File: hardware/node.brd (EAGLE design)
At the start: 39.4 x 25.7 mm, 74 parts, among them IC1 MAX1555, IC2 TS5205, Q1 P-MOSFET, U1 ATMEGA32U4, U2 MCP1703CB/TOREX-XC6206, Y1 8MHz

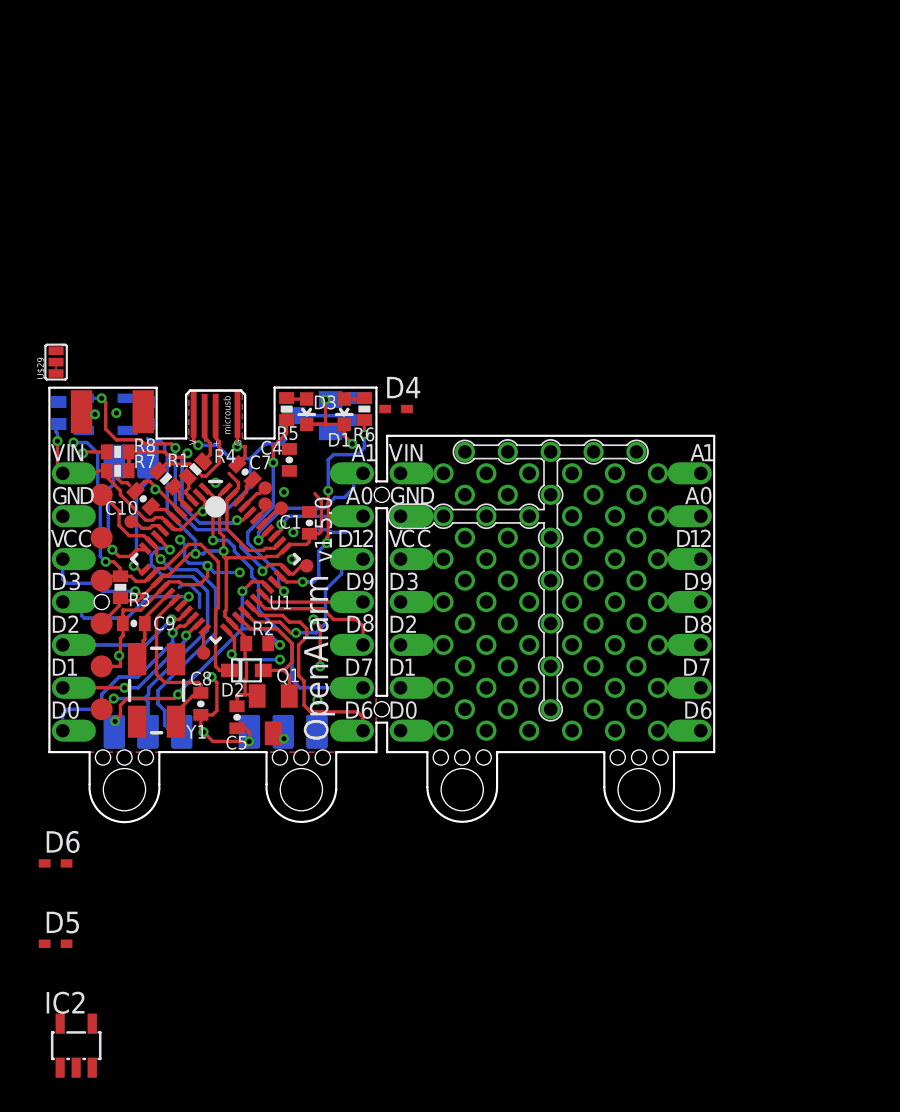
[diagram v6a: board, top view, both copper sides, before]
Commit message: Node + Proto Shield + Lipo Shield
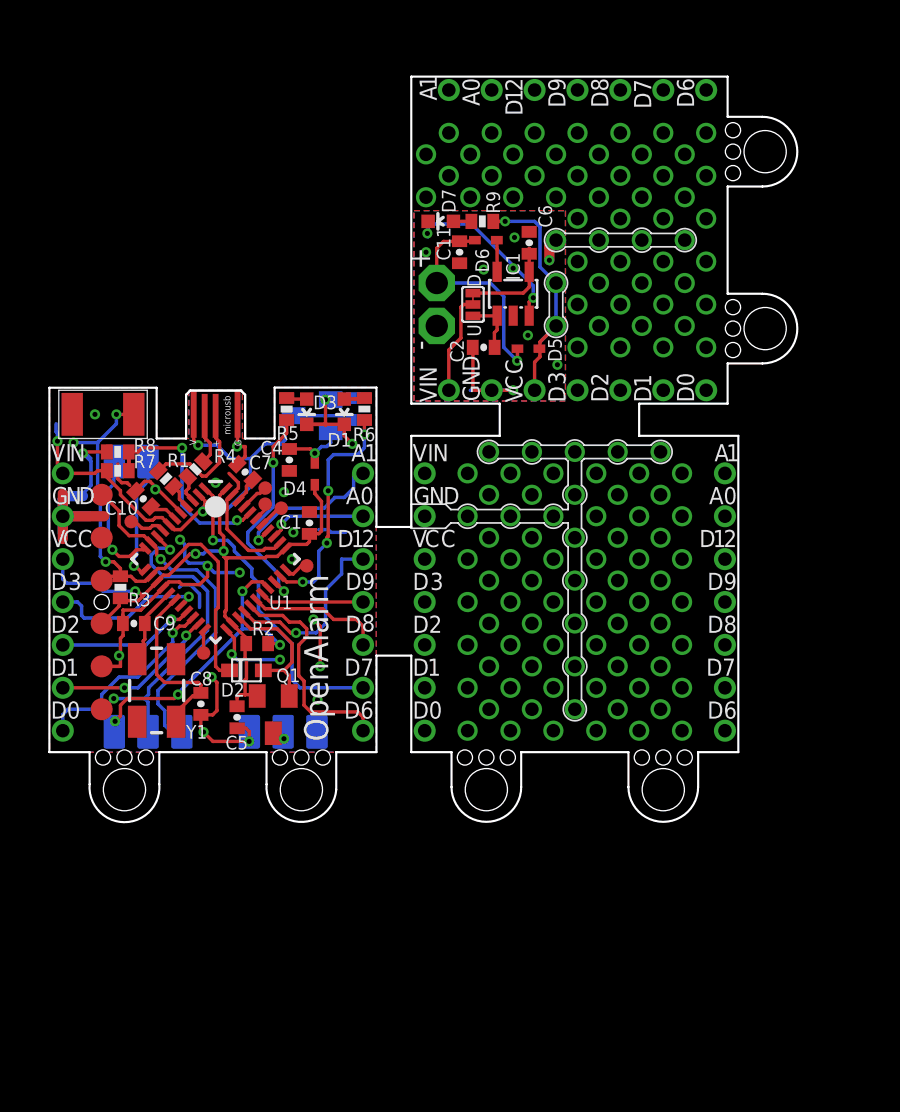
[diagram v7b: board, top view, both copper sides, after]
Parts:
- removed IC2: TS5205, v-reg:SOT25
- added C11: 1uF, SparkFun:0402-CAP
- added D7: Green, SparkFun:LED-0603
- added LIPO+, LIPO-: TPPAD1-13, testpad:P1-13
- added R9: 330, SparkFun:0402-RES
- added U$30, U$31, U$32, U$33, U$34, U$35, U$36, U$37, U$38, U$39, U$40, U$41, U$42, U$43: IOPAD, openalarm:IOPAD
- moved D5 45.1 mm to (28.4, 23.9), turned to 180 degrees
- moved D6 44.8 mm to (25.8, 30.3)
- moved C2 25.5 mm to (25.7, 24.0), flipped to the top, turned to 0 degrees
- moved IC1 25.2 mm to (27.5, 27.1), flipped to the top, turned to 0 degrees
- moved U$29 24.9 mm to (25.1, 26.5), turned to 270 degrees
- moved C6 24.8 mm to (28.4, 30.2), flipped to the top
- moved D4 6.15 mm to (15.7, 16.4), turned to 90 degrees
- moved U$15 1.43 mm to (22.7, 16.5)
- moved U$16 1.43 mm to (22.7, 14.0)
- moved U$17 1.43 mm to (22.7, 11.4)
- moved U$18 1.43 mm to (22.7, 8.89)
- moved U$19 1.43 mm to (22.7, 6.35)
- moved U$20 1.43 mm to (22.7, 3.81)
- moved U$21 1.43 mm to (22.7, 1.27)
- moved U$22 1.43 mm to (39.5, 1.27)
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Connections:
- removed net CHG: IC1.3, TP12.TP, U1.33
- removed net N$12: C6.2, D5.A, D6.C
- removed net N$14: IC1.4, U$29.C0
- removed net N$15: C2.2, U$29.COM
- new net N$133: D7.C, IC1.3
- new net N$178: C6.2, IC1.4, U$29.C0
- new net N$179: C2.2, IC1.1, U$29.C1
- new net N$181: U$33.P$1
- new net N$182: U$34.P$1
- new net N$183: U$35.P$1
- new net N$184: U$36.P$1
- new net N$185: U$38.P$1
- new net N$186: U$39.P$1
- new net N$187: U$40.P$1
- new net N$188: U$41.P$1
- new net N$189: U$42.P$1
- new net N$190: U$43.P$1
- new net N$191: U$37.P$1
- new net N$192: C11.2, D5.A, D6.C, LIPO+.TP
- new net SL_GND: C11.1, C2.1, C6.1, IC1.2, LIPO-.TP, U$31.P$1
- new net SL_VBUS: U$29.COM, U$30.P$1
- new net SL_VCC: D5.C, R9.2, U$32.P$1
- new net _CHG: TP12.TP, U1.33
- net A0: now also U$9.P$1; no longer U$9.P$2
- net A1: now also U$8.P$1; no longer U$8.P$2
- net D0: now also U$2.P$1; no longer U$2.P$2
- net D1: now also U$1.P$1; no longer U$1.P$2
- net D12: now also U$10.P$1; no longer U$10.P$2
- net D2: now also U$3.P$1; no longer U$3.P$2
- net D3: now also U$4.P$1; no longer U$4.P$2
- net D6: now also U$14.P$1; no longer U$14.P$2
- net D7: now also U$13.P$1; no longer U$13.P$2
- net D8: now also U$12.P$1; no longer U$12.P$2
- net D9: now also U$11.P$1; no longer U$11.P$2
- net GND: now also U$6.P$1; no longer C2.1, C6.1, IC1.2, U$6.P$2
- net N$11: now also D7.A, R9.1; no longer IC1.1, U$29.C1
- net N$13: now also U$16.P$1; no longer U$16.P$2
- net N$27: now also U$17.P$1; no longer U$17.P$2
- net N$29: now also U$18.P$1; no longer U$18.P$2
- net N$30: now also U$19.P$1; no longer U$19.P$2
- net N$31: now also U$20.P$1; no longer U$20.P$2
- net N$32: now also U$21.P$1; no longer U$21.P$2
- net N$40: now also U$23.P$1; no longer U$23.P$2
- net N$41: now also U$24.P$1; no longer U$24.P$2
- net N$42: now also U$25.P$1; no longer U$25.P$2
- net N$43: now also U$26.P$1; no longer U$26.P$2
- net N$44: now also U$27.P$1; no longer U$27.P$2
- net N$45: now also U$28.P$1; no longer U$28.P$2
- net N$46: now also U$22.P$1; no longer U$22.P$2
- net N$9: now also U$15.P$1; no longer U$15.P$2
- net VBUS: now also U$7.P$1; no longer U$7.P$2
- net VCC: now also U$5.P$1; no longer U$5.P$2
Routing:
- net CHG: track 21.4 -> 0.00 mm, vias 3 -> 0
- net SL_VCC: track 0.00 -> 14.9 mm, vias 0 -> 3
- net N$192: track 0.00 -> 13.7 mm, vias 0 -> 1
- net GND: track 61.0 -> 74.3 mm, vias 23 -> 22
- net N$133: track 0.00 -> 11.3 mm, vias 0 -> 2
- net SL_GND: track 0.00 -> 8.98 mm, vias 0 -> 12
- net VCC: track 48.5 -> 40.6 mm
- net N$178: track 0.00 -> 6.08 mm
- net SL_VBUS: track 0.00 -> 6.00 mm
- net VBAT: track 0.00 -> 4.03 mm, vias 0 -> 1
- net RESET: track 25.5 -> 29.0 mm, vias 2 -> 3
- net N$179: track 0.00 -> 3.38 mm
- net N$180: track 0.00 -> 1.88 mm
- net _CHG: track 0.00 -> 1.58 mm
- net N$11: track 0.00 -> 1.06 mm
- added copper zone on layer 1, net SL_GND
- added copper zone on layer 16, net SL_GND
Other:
- board size 39.4 x 25.7 mm -> 44.3 x 44.2 mm
- board text added: "+"
- board text added: "-"
- board text added: "OpenAlarm Shield Lipo"
- board text added: "U"
- board text added: "oa node v1.5.0"
- board text removed: "oa node"
- board text removed: "v1.5.0"

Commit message: Node + 2 Proto Shield + Lipo Shield
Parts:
- added U$44, U$45, U$46, U$47, U$48, U$49, U$50, U$51, U$52, U$53, U$54, U$55, U$56, U$57: IOPAD, openalarm:IOPAD
- moved U$41 37.7 mm to (1.27, 24.3), turned to 0 degrees
- moved U$38 35.4 mm to (1.27, 26.8), turned to 0 degrees
- moved U$34 33.4 mm to (1.27, 29.4), turned to 0 degrees
- moved U$35 31.6 mm to (1.27, 31.9), turned to 0 degrees
- moved U$32 30.2 mm to (1.27, 34.4), turned to 0 degrees
- moved U$31 29.1 mm to (1.27, 37.0), turned to 0 degrees
- moved U$30 28.5 mm to (1.27, 39.5), turned to 0 degrees
- moved D5 27.4 mm to (3.25, 34.8), turned to 90 degrees
- moved C2 26.1 mm to (3.33, 37.5), turned to 270 degrees
- moved U$43 25.3 mm to (18.1, 24.3), turned to 180 degrees
- moved LIPO- 23.7 mm to (4.60, 40.2), turned to 0 degrees
- moved IC1 22.6 mm to (6.51, 35.7), turned to 270 degrees
- moved U$29 22.4 mm to (5.87, 38.1), turned to 180 degrees
- moved U$40 21.8 mm to (18.1, 26.8), turned to 180 degrees
- moved LIPO+ 20.1 mm to (7.14, 40.2), turned to 0 degrees
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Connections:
- new net N$245: U$44.P$1
- new net N$246: U$45.P$1
- new net N$247: U$46.P$1
- new net N$248: U$47.P$1
- new net N$249: U$48.P$1
- new net N$250: U$49.P$1
- new net N$251: U$50.P$1
- new net N$252: U$52.P$1
- new net N$253: U$53.P$1
- new net N$254: U$54.P$1
- new net N$255: U$55.P$1
- new net N$256: U$56.P$1
- new net N$257: U$57.P$1
- new net N$258: U$51.P$1
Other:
- board size 44.3 x 44.2 mm -> 40.8 x 45.9 mm
- board text added: "OpenAlarm Lipo Shield v1.0.0"
- board text removed: "OpenAlarm Shield Lipo"
